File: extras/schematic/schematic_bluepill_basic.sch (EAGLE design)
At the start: 19 parts, among them U1 SI4735-D60-GU

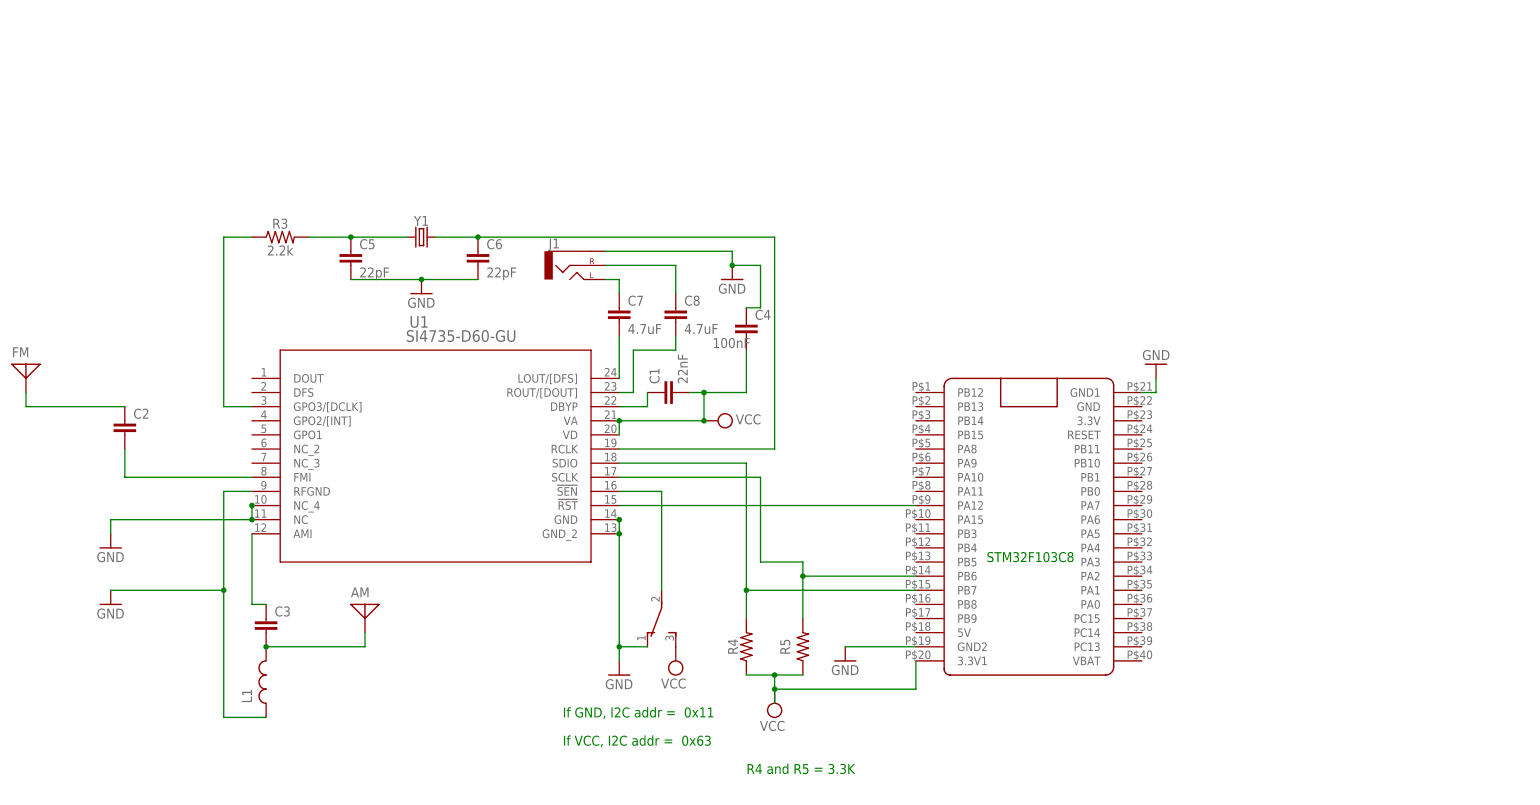
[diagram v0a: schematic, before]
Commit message: SI473X Arduino Library
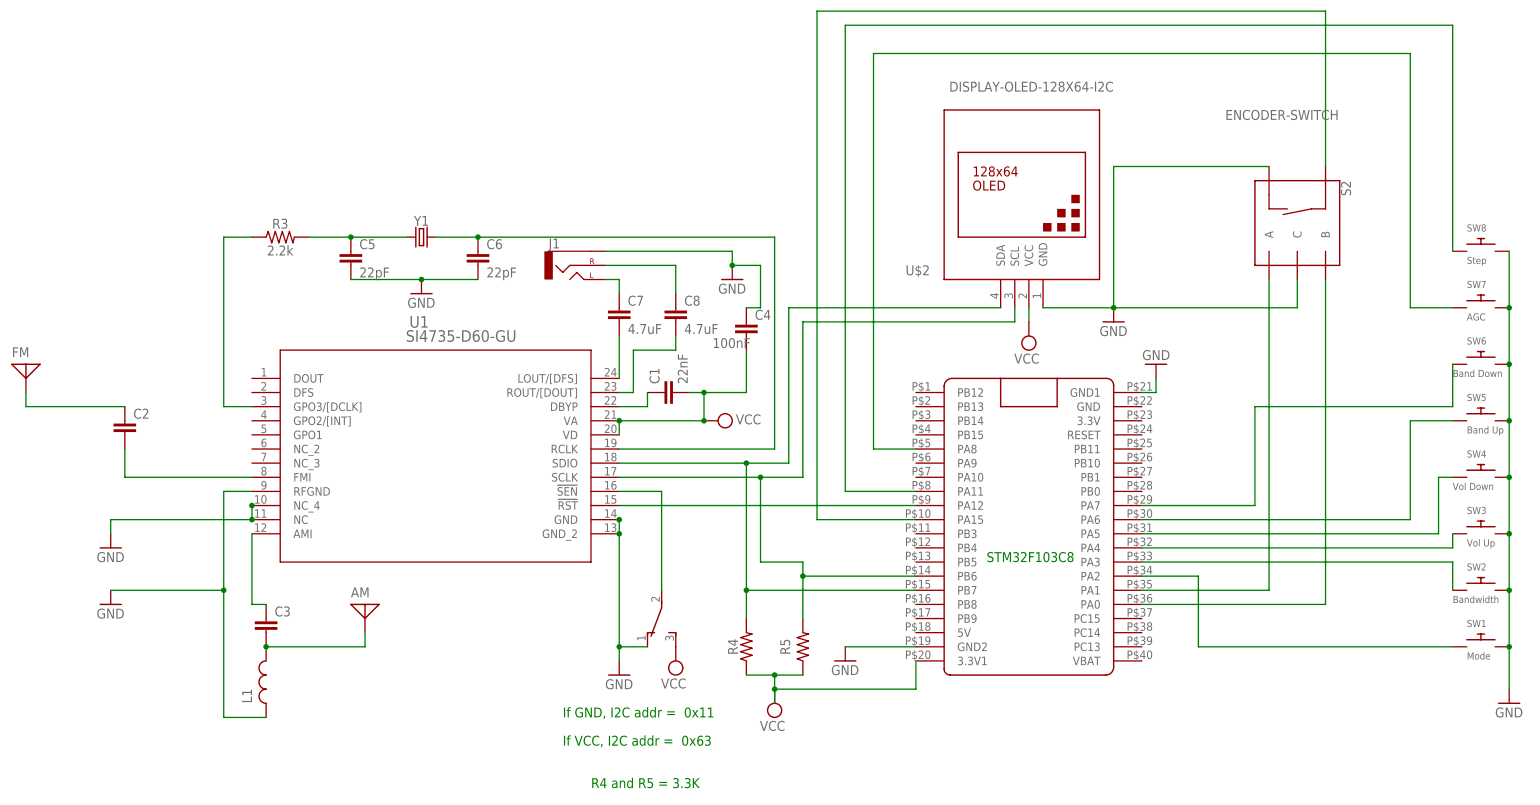
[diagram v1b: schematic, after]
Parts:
- added S2: ENCODER-SWITCH, SparkFun-Switches:ENCODER-SWITCH
- added SW1: Mode, adafruit:SWITCH_PUSHBUTTONEVQ-PE
- added SW2: Bandwidth, adafruit:SWITCH_PUSHBUTTONEVQ-PE
- added SW3: Vol Up, adafruit:SWITCH_PUSHBUTTONEVQ-PE
- added SW4: Vol Down, adafruit:SWITCH_PUSHBUTTONEVQ-PE
- added SW5: Band Up, adafruit:SWITCH_PUSHBUTTONEVQ-PE
- added SW6: Band Down, adafruit:SWITCH_PUSHBUTTONEVQ-PE
- added SW7: AGC, adafruit:SWITCH_PUSHBUTTONEVQ-PE
- added SW8: Step, adafruit:SWITCH_PUSHBUTTONEVQ-PE
- added U$2: DISPLAY-OLED-128X64-I2C, diy-modules:DISPLAY-OLED-128X64-I2C
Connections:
- new net N$16: S2.SW+, U$1.PA15
- new net N$17: S2.B, U$1.PA0
- new net N$18: S2.A, U$1.PA1
- new net N$19: SW1.P$1, U$1.PA2
- new net N$20: SW2.P$1, U$1.PA3
- new net N$21: SW3.P$1, U$1.PA4
- new net N$22: SW4.P$1, U$1.PA5
- new net N$23: SW5.P$1, U$1.PA6
- new net N$24: SW6.P$1, U$1.PA7
- new net N$25: SW7.P$1, U$1.PA8
- new net N$26: SW8.P$1, U$1.PA11
- net GND: now also S2.C, S2.SW-, SW1.P$2, SW2.P$2, SW3.P$2, SW4.P$2, SW5.P$2, SW6.P$2, SW7.P$2, SW8.P$2, U$2.GND
- net N$15: now also U$2.SDA
- net SDA: now also U$2.SCL
- net VCC: now also U$2.VCC

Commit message: SI473X Arduino Library
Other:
- note added: "Optional"
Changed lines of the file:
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@@
 <text x="27.94" y="43.18" size="1.778" layer="91">R4 and R5 = 3.3K</text>
 <text x="99.06" y="83.82" size="1.778" layer="91">STM32F103C8</text>
+<rectangle x1="-35.56" y1="137.16" x2="-20.32" y2="147.32" layer="205"/>
+<text x="-30.48" y="149.86" size="1.778" layer="205">Optional</text>
 </plain>
 <instances>
